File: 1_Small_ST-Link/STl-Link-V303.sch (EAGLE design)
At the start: 31 parts

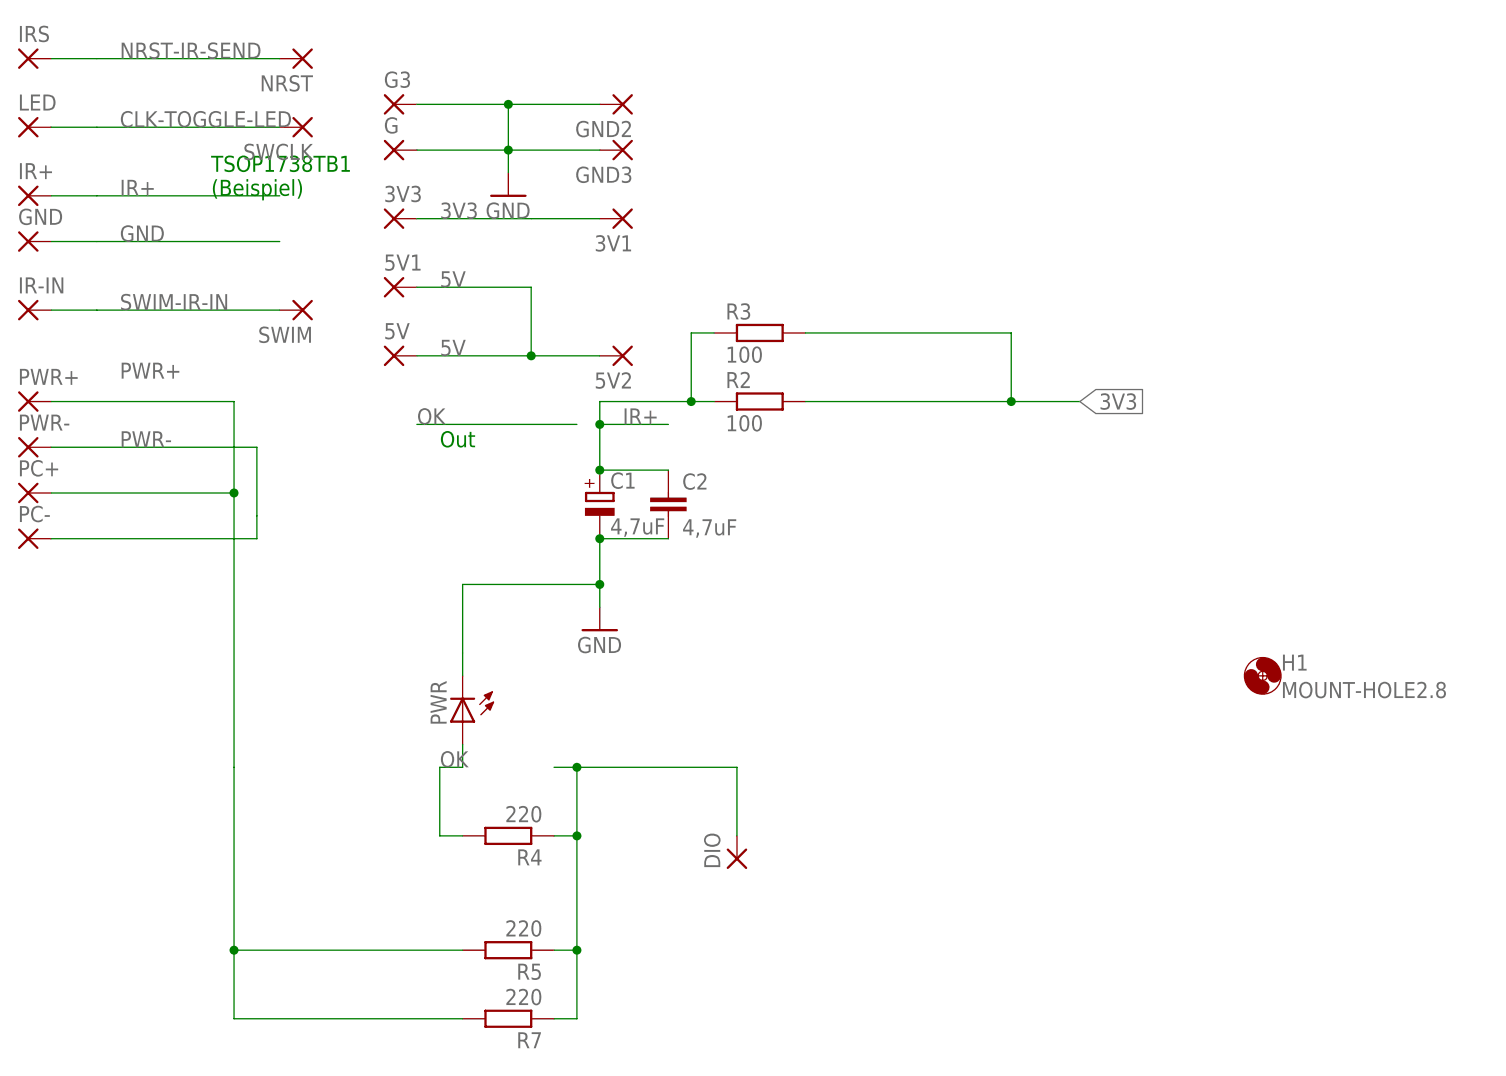
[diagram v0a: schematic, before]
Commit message: LED removed
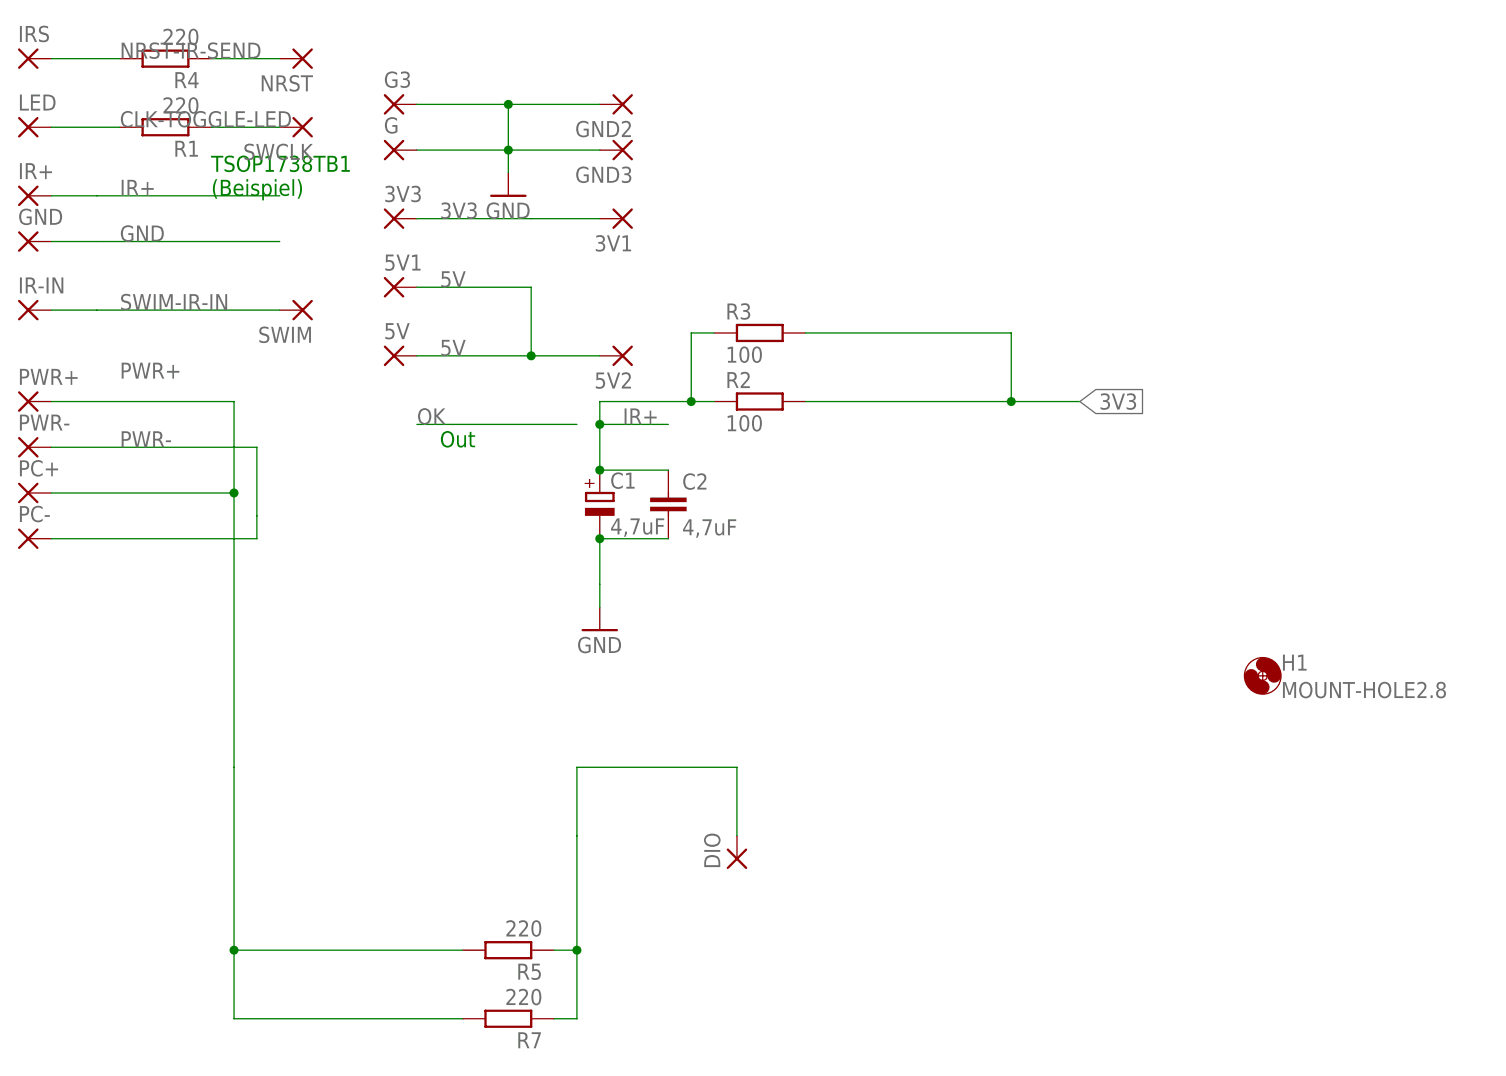
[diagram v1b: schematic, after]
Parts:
- removed PWR: (no value), led:LEDCHIPLED_1206
- added R1: 220, rcl:R-EU_R0805W
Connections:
- removed net OK: PWR.A, R4.2
- new net N$1: NRST.P, R4.1
- new net N$2: LED.P, R1.2
- net CLK-TOGGLE-LED: now also R1.1; no longer LED.P
- net DIO-EINSCH: no longer R4.1
- net GND: no longer PWR.C
- net NRST-IR-SEND: now also R4.2; no longer NRST.P
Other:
- moved on the sheet: R4
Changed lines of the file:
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@@
 <class number="0" name="default" width="0.4064" drill="0">
+</class>
+<class number="1" name="Power" width="0.6096" drill="0">
 </class>
 </classes>
@@
 <part name="R4" library="rcl" deviceset="R-EU_" device="R0805W" value="220"/>
 <part name="C2" library="rcl" deviceset="C-EU" device="C1206K" value="4,7uF"/>
-<part name="PWR" library="led" deviceset="LED" device="CHIPLED_1206"/>
 <part name="LED" library="wirepad" deviceset="SMD2" device=""/>
 <part name="IR+" library="wirepad" deviceset="SMD2" device=""/>
@@
 <part name="GND3" library="wirepad" deviceset="SMD2" device=""/>
 <part name="SWCLK" library="wirepad" deviceset="SMD2" device=""/>
+<part name="R1" library="rcl" deviceset="R-EU_" device="R0805W" value="220"/>
 </parts>
 <sheets>
@@
 <instance part="H1" gate="G$1" x="185.42" y="33.02"/>
 <instance part="R3" gate="G$1" x="129.54" y="71.12"/>
-<instance part="R4" gate="G$1" x="101.6" y="15.24" rot="R180"/>
+<instance part="R4" gate="G$1" x="63.5" y="101.6" rot="R180"/>
 <instance part="C2" gate="G$1" x="119.38" y="53.34"/>
-<instance part="PWR" gate="G$1" x="96.52" y="27.94" rot="R180"/>
 <instance part="LED" gate="1" x="48.26" y="93.98"/>
 <instance part="IR+" gate="1" x="48.26" y="86.36"/>
@@
 <instance part="GND3" gate="1" x="114.3" y="91.44" rot="R180"/>
 <instance part="SWCLK" gate="1" x="78.74" y="93.98" rot="R180"/>
+<instance part="R1" gate="G$1" x="63.5" y="93.98" rot="R180"/>
 </instances>
 <busses>
 </busses>
 <nets>
-<net name="5V" class="0">
+<net name="5V" class="1">
 <segment>
 <pinref part="5V1" gate="1" pin="P"/>
@@
 <net name="CLK-TOGGLE-LED" class="0">
 <segment>
-<wire x1="76.2" y1="93.98" x2="55.88" y2="93.98" width="0.1524" layer="91"/>
+<wire x1="76.2" y1="93.98" x2="68.58" y2="93.98" width="0.1524" layer="91"/>
 <label x="58.42" y="93.98" size="1.778" layer="95"/>
-<pinref part="LED" gate="1" pin="P"/>
-<wire x1="50.8" y1="93.98" x2="55.88" y2="93.98" width="0.1524" layer="91"/>
 <pinref part="SWCLK" gate="1" pin="P"/>
-</segment>
-</net>
-<net name="GND" class="0">
+<pinref part="R1" gate="G$1" pin="1"/>
+</segment>
+</net>
+<net name="GND" class="1">
 <segment>
 <pinref part="C1" gate="G$1" pin="-"/>
@@
 <wire x1="119.38" y1="48.26" x2="111.76" y2="48.26" width="0.1524" layer="91"/>
 <junction x="111.76" y="48.26"/>
-<pinref part="PWR" gate="G$1" pin="C"/>
-<wire x1="96.52" y1="33.02" x2="96.52" y2="35.56" width="0.1524" layer="91"/>
-<wire x1="96.52" y1="35.56" x2="96.52" y2="43.18" width="0.1524" layer="91"/>
-<wire x1="96.52" y1="43.18" x2="111.76" y2="43.18" width="0.1524" layer="91"/>
-<junction x="111.76" y="43.18"/>
 </segment>
 <segment>
@@
 <net name="NRST-IR-SEND" class="0">
 <segment>
-<wire x1="76.2" y1="101.6" x2="55.88" y2="101.6" width="0.1524" layer="91"/>
 <label x="58.42" y="101.6" size="1.778" layer="95"/>
 <pinref part="IRS" gate="1" pin="P"/>
-<wire x1="50.8" y1="101.6" x2="55.88" y2="101.6" width="0.1524" layer="91"/>
-<pinref part="NRST" gate="1" pin="P"/>
+<wire x1="50.8" y1="101.6" x2="58.42" y2="101.6" width="0.1524" layer="91"/>
+<pinref part="R4" gate="G$1" pin="2"/>
 </segment>
 </net>
@@
 <net name="OK" class="0">
 <segment>
-<wire x1="93.98" y1="22.86" x2="96.52" y2="22.86" width="0.1524" layer="91"/>
-<pinref part="R4" gate="G$1" pin="2"/>
-<wire x1="96.52" y1="15.24" x2="93.98" y2="15.24" width="0.1524" layer="91"/>
-<wire x1="93.98" y1="15.24" x2="93.98" y2="22.86" width="0.1524" layer="91"/>
-<pinref part="PWR" gate="G$1" pin="A"/>
-<wire x1="96.52" y1="22.86" x2="96.52" y2="25.4" width="0.1524" layer="91"/>
-<label x="93.98" y="22.86" size="1.778" layer="95"/>
-</segment>
-<segment>
 <wire x1="91.44" y1="60.96" x2="109.22" y2="60.96" width="0.1524" layer="91"/>
 <label x="91.44" y="60.96" size="1.778" layer="95"/>
@@
 <net name="DIO-EINSCH" class="0">
 <segment>
-<wire x1="106.68" y1="22.86" x2="109.22" y2="22.86" width="0.1524" layer="91"/>
-<pinref part="R4" gate="G$1" pin="1"/>
-<wire x1="106.68" y1="15.24" x2="109.22" y2="15.24" width="0.1524" layer="91"/>
 <wire x1="109.22" y1="15.24" x2="109.22" y2="22.86" width="0.1524" layer="91"/>
 <wire x1="127" y1="22.86" x2="109.22" y2="22.86" width="0.1524" layer="91"/>
-<junction x="109.22" y="22.86"/>
 <wire x1="109.22" y1="15.24" x2="109.22" y2="2.54" width="0.1524" layer="91"/>
-<junction x="109.22" y="15.24"/>
 <pinref part="R5" gate="G$1" pin="1"/>
 <wire x1="109.22" y1="2.54" x2="106.68" y2="2.54" width="0.1524" layer="91"/>
@@
 </segment>
 </net>
+<net name="N$1" class="0">
+<segment>
+<wire x1="76.2" y1="101.6" x2="68.58" y2="101.6" width="0.1524" layer="91"/>
+<pinref part="NRST" gate="1" pin="P"/>
+<pinref part="R4" gate="G$1" pin="1"/>
+</segment>
+</net>
+<net name="N$2" class="0">
+<segment>
+<pinref part="LED" gate="1" pin="P"/>
+<wire x1="50.8" y1="93.98" x2="58.42" y2="93.98" width="0.1524" layer="91"/>
+<pinref part="R1" gate="G$1" pin="2"/>
+</segment>
+</net>
